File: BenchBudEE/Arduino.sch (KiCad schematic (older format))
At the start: 0 parts

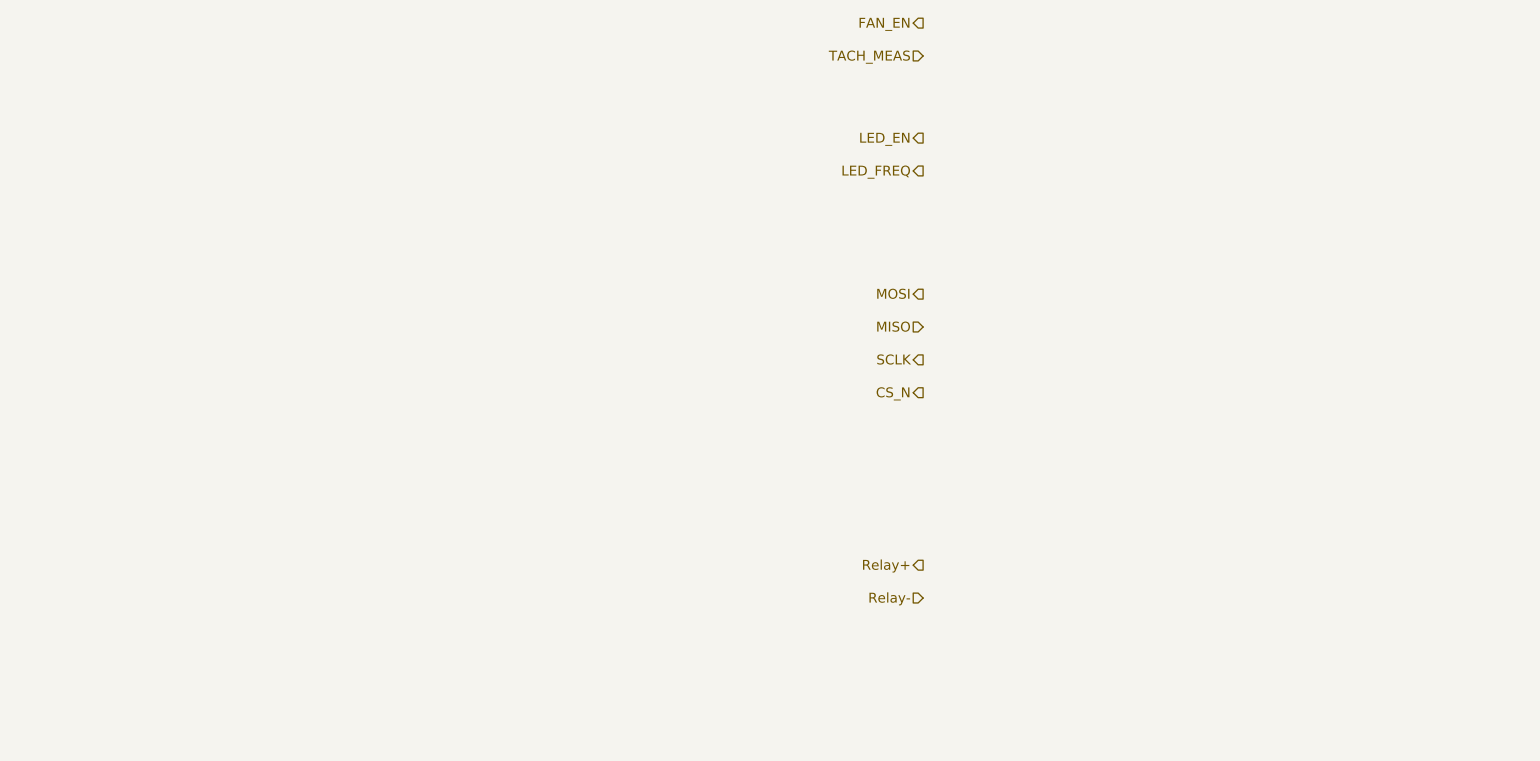
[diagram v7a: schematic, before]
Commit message: Populated the Arduino block and top level wiring.
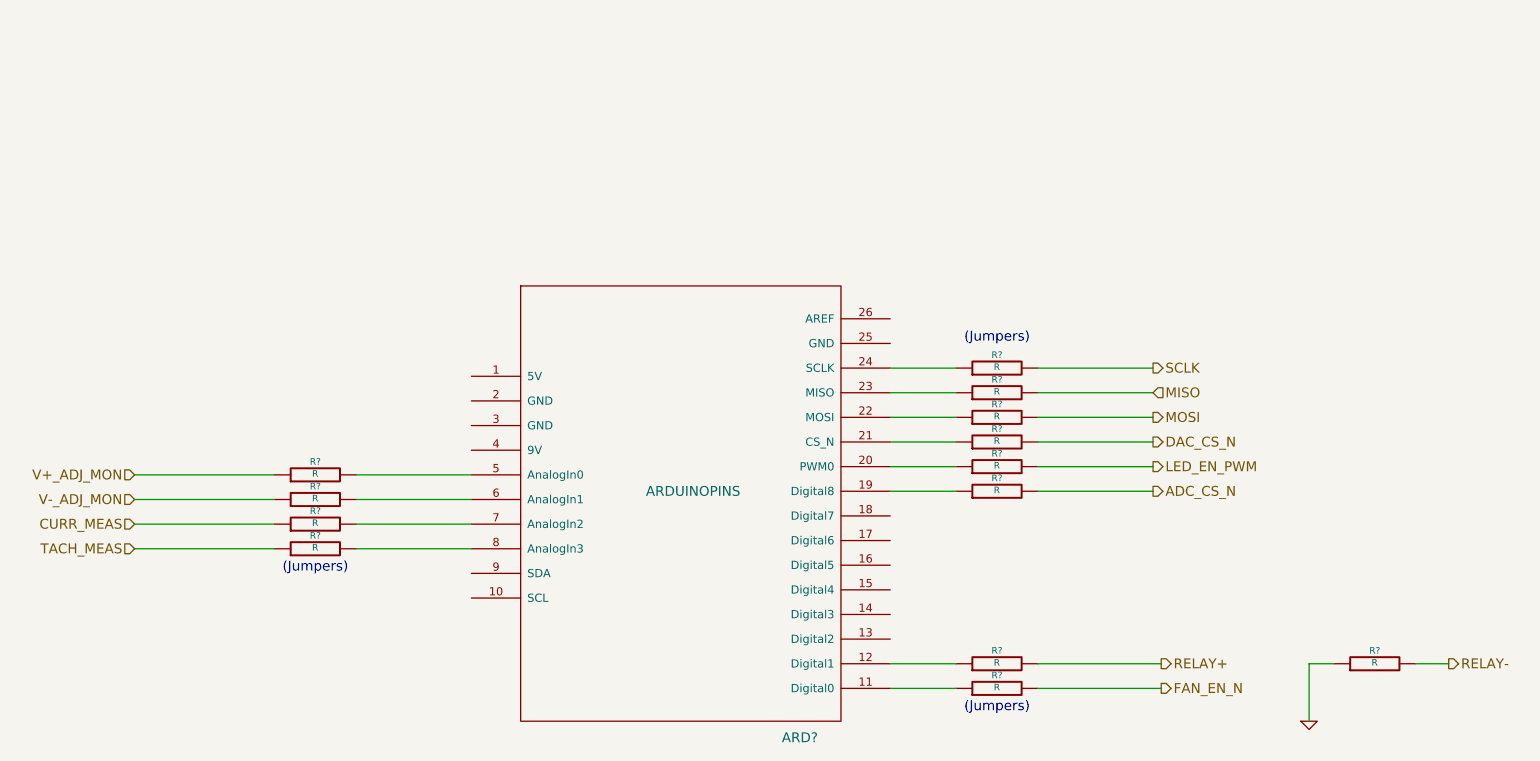
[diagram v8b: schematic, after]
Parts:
- added ARD?: ARDUINOPINS, symbol ARDUINOPINS
- added R? (x13): R, ~, symbol R
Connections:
- net MISO: now also R?.2
- net MOSI: now also R?.2
- net SCLK: now also R?.2
- net TACH_MEAS: now also R?.1
- new net: ARD?.11 (Digital0), R?.1
- new net: ARD?.12 (Digital1), R?.1
- new net: ARD?.19 (Digital8), R?.1
- new net: ARD?.20 (PWM0), R?.1
- new net: ARD?.21 (CS_N), R?.1
- new net: ARD?.22 (MOSI), R?.1
- new net: ARD?.23 (MISO), R?.1
- new net: ARD?.24 (SCLK), R?.1
- new net: ARD?.5 (AnalogIn0), R?.2
- new net: ARD?.6 (AnalogIn1), R?.2
- new net: ARD?.7 (AnalogIn2), R?.2
- new net: ARD?.8 (AnalogIn3), R?.2
- new net ADC_CS_N: R?.2
- new net CURR_MEAS: R?.1
- new net DAC_CS_N: R?.2
- new net FAN_EN_N: R?.2
- new net GND: R?.1
- new net LED_EN_PWM: R?.2
- new net RELAY+: R?.2
- new net RELAY-: R?.2
- new net V+_ADJ_MON: R?.1
- new net V-_ADJ_MON: R?.1
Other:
- note added: "(Jumpers)"
